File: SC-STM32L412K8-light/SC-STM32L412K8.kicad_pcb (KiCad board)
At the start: 2 copper layers, 31.6 x 15.1 mm, 62 parts, among them J1 usb, J11 Vibro, J12 +3v, J13 +vibro, J2 +29.6 SiPM, J3 TxD, J4 RxD, J5 SWDIO, J6 SWCLK, J7 +BAT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

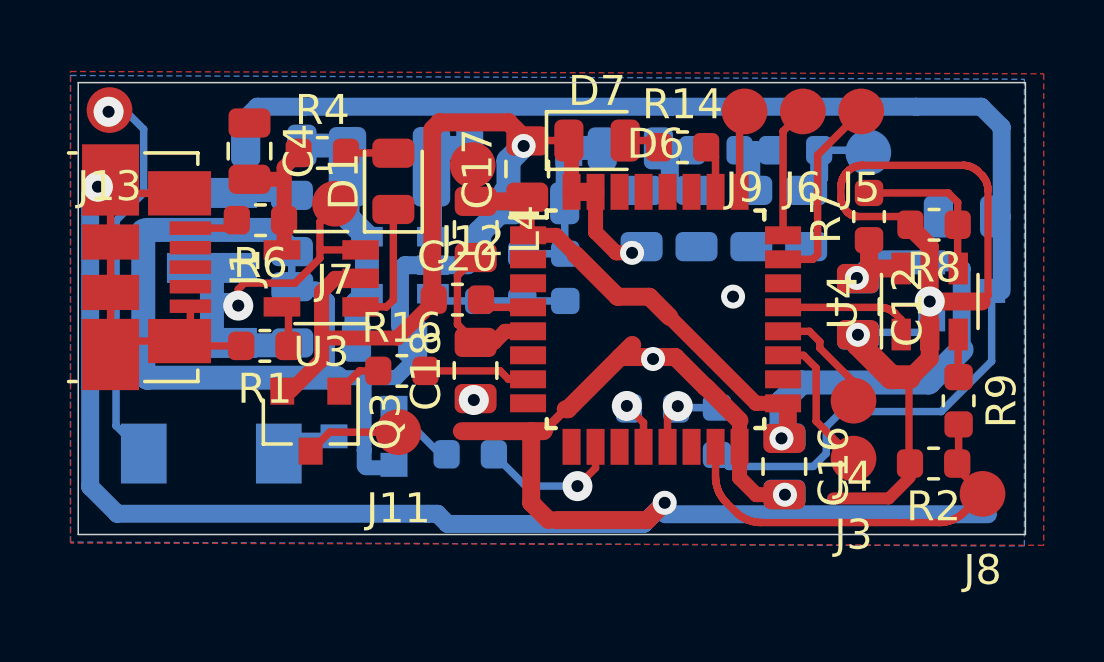
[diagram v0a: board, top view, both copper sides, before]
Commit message: изменено:      SC-STM32L412K8-light/SC-STM32L412K8.kicad_pcb 	изменено:      SC-STM32L412K8-light/SC-STM32L412K8.kicad_pcb-bak 	изменено:      SC-STM32L412K8-light/SC-STM32L412K8.net 	изменено:      SC-STM32L412K8-light/SC-STM32L412K8.sch 	изменено:      SC-STM32L412K8-light/SC-STM32L412K8.sch-bak 	изменено:      STM32L412K8code/Release/Core/Src/stm32l4xx_it.su
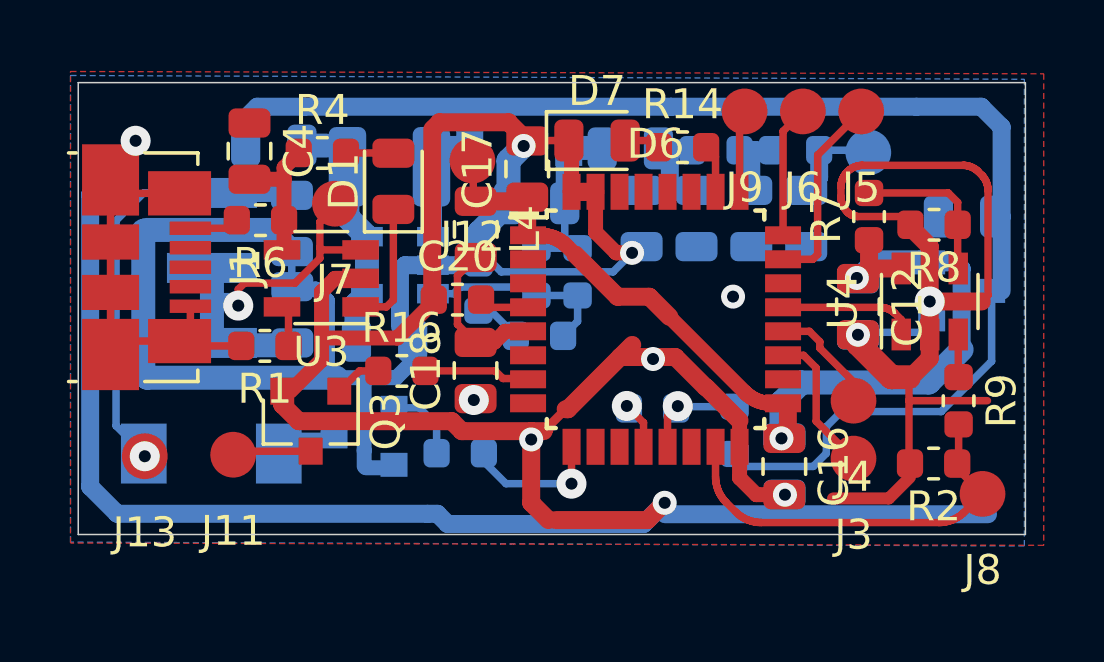
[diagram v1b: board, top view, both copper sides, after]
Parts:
- added R10: 1k*, Resistor_SMD:R_0603_1608Metric, B.Cu at (40.8, 59.7)
- moved J13 11.6 mm to (29.7, 65.3)
- moved J11 5.56 mm to (32.6, 65.3)
- moved R3 2.80 mm to (42.8, 61.3), turned to 180 degrees
- moved R19 0.58 mm to (49.3, 64.5)
- moved C5 0.51 mm to (42.7, 59.2)
- moved R5 0.45 mm to (44.1, 59.2)
- moved R15 0.33 mm to (40.2, 65.2)
- moved J12 0.15 mm to (40.6, 55.5)
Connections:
- D6 pad 10: Buzer -> (no net)
- D6 pad 9: (no net) -> Buzer
- R3 pad 2: GND -> Net-(R10-Pad1)
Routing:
- net GND: track 174.4 -> 189.3 mm, vias 10 -> 11
- net +BATT: track 65.6 -> 61.5 mm
- net Net-(C5-Pad2): track 4.51 -> 6.57 mm
- net Net-(R10-Pad1): track 0.00 -> 1.59 mm
- net bl: track 2.99 -> 3.56 mm
- net Net-(J11-Pad1): track 3.18 -> 2.63 mm

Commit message: изменено:      SC-STM32L412K8-light/SC-STM32L412K8-cache.lib 	изменено:      SC-STM32L412K8-light/SC-STM32L412K8.kicad_pcb 	изменено:      SC-STM32L412K8-light/SC-STM32L412K8.kicad_pcb-bak 	изменено:      SC-STM32L412K8-light/SC-STM32L412K8.net 	изменено:      SC-STM32L412K8-light/SC-STM32L412K8.sch 	изменено:      SC-STM32L412K8-light/SC-STM32L412K8.sch-bak
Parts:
- removed BZ1: Buzzer, My-library:BuzerSMD
- removed Q3: KT231Г9, Package_TO_SOT_SMD:SOT-23
- added J10: Buzzer, My-library:SMD-CONN, B.Cu at (36.6, 65.3)
- added Q1: 2N7002, Package_TO_SOT_SMD:SOT-23, F.Cu at (36.8, 64.2)
- added R12: 200, Resistor_SMD:R_0603_1608Metric, B.Cu at (38.1, 65.3)
- J11, J13: moved to B.Cu
- Q2: value KT231Г9 -> 2N7002
- R10: value 1k* -> 3k*
- R15, R16: value 4.7k -> 100k
- moved J13 11.0 mm to (31.4, 54.5)
- moved R15 4.63 mm to (44.7, 66.2), turned to 180 degrees
- moved Q2 3.59 mm to (40.3, 66.1)
- moved J11 2.03 mm to (34.6, 65.3)
- moved R10 1.64 mm to (40.6, 61.3), turned to 180 degrees
- moved R16 1.26 mm to (39.0, 63.5), turned to 90 degrees
- moved R19 1.07 mm to (49.2, 63.4), turned to 0 degrees
- moved R3 0.58 mm to (43.4, 61.3)
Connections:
- Q2 pad 1: Net-(Q2-Pad1) -> Buzer
- R15 pad 1: Net-(Q2-Pad1) -> GND
- R16 pad 1: Net-(Q3-Pad1) -> GND
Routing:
- net +BATT: track 61.5 -> 52.5 mm, vias 1 -> 0
- net GND: track 189.3 -> 193.2 mm, vias 11 -> 10
- net Net-(Q2-Pad1): track 2.60 -> 0.00 mm
- net Net-(J10-Pad1): track 0.00 -> 1.87 mm
- net Vibro: track 3.53 -> 5.14 mm
- net Net-(Q3-Pad1): track 1.58 -> 0.00 mm
- net Net-(Q2-Pad3): track 2.08 -> 1.13 mm
- net Net-(C12-Pad1): track 35.1 -> 34.4 mm
- net bl: track 3.56 -> 2.85 mm
- net Net-(J11-Pad1): track 2.63 -> 2.15 mm, vias 0 -> 1

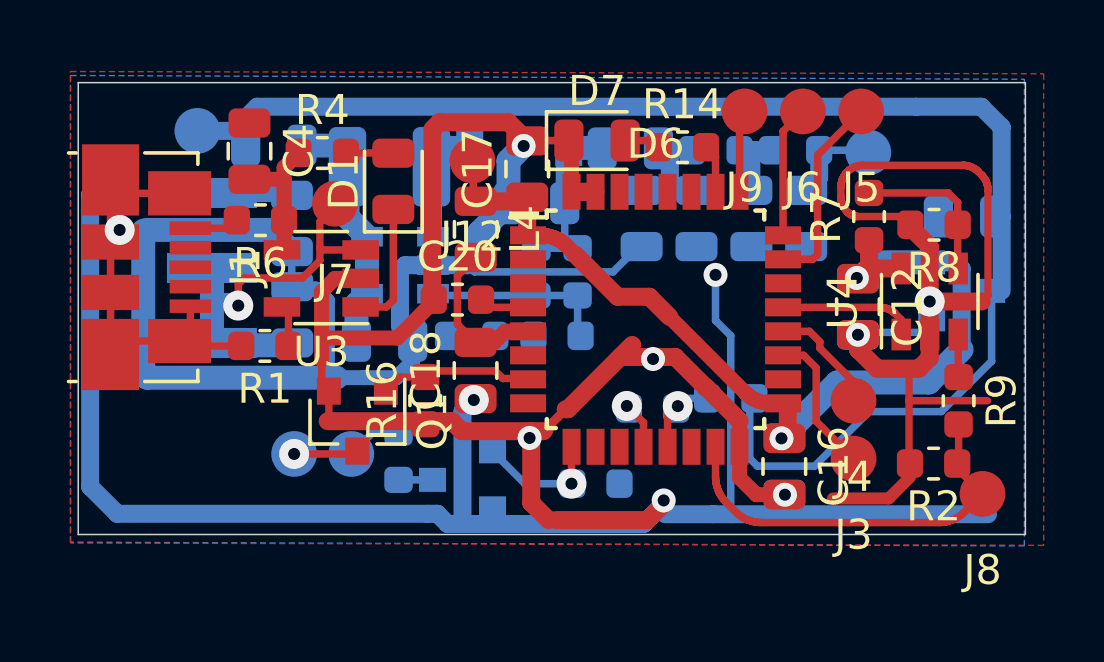
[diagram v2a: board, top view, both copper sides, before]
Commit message: modified:   FreeCAD/sc-box-7.FCStd 	modified:   FreeCAD/sc-box-7.stl 	modified:   FreeCAD/sc-cover-7.FCStd 	modified:   FreeCAD/sc-cover-7.FCStd1 	modified:   FreeCAD/sc-cover-7.stl 	modified:   SC-STM32L412K8-light/SC-STM32L412K8.kicad_pcb 	modified:   SC-STM32L412K8-light/SC-STM32L412K8.kicad_pcb-bak 	modified:   SC-STM32L412K8-light/SC-STM32L412K8.net 	modified:   SC-STM32L412K8-light/SC-STM32L412K8.sch 	modified:   SC-STM32L412K8-light/SC-STM32L412K8.sch-bak
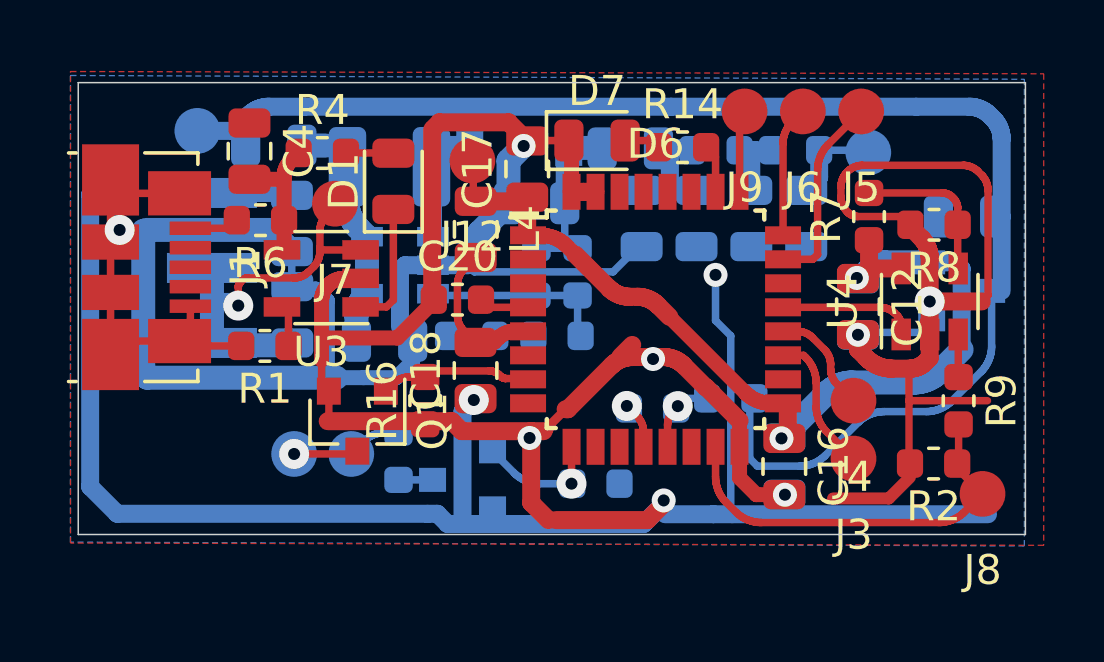
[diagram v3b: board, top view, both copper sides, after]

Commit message: изменено:      AndroidDoZer/app/src/main/java/ru/starline/dozer/FullscreenActivity2.java 	изменено:      AndroidDoZer/app/src/main/res/layout/activity_fullscreen2.xml 	изменено:      SC-STM32L412K8-light/SC-STM32L412K8-cache.lib 	изменено:      SC-STM32L412K8-light/SC-STM32L412K8.kicad_pcb 	изменено:      SC-STM32L412K8-light/SC-STM32L412K8.kicad_pcb-bak 	изменено:      SC-STM32L412K8-light/SC-STM32L412K8.net 	изменено:      SC-STM32L412K8-light/SC-STM32L412K8.sch 	изменено:      SC-STM32L412K8-light/SC-STM32L412K8.sch-bak 	изменено:      STM32L412K8code/.settings/language.settings.xml
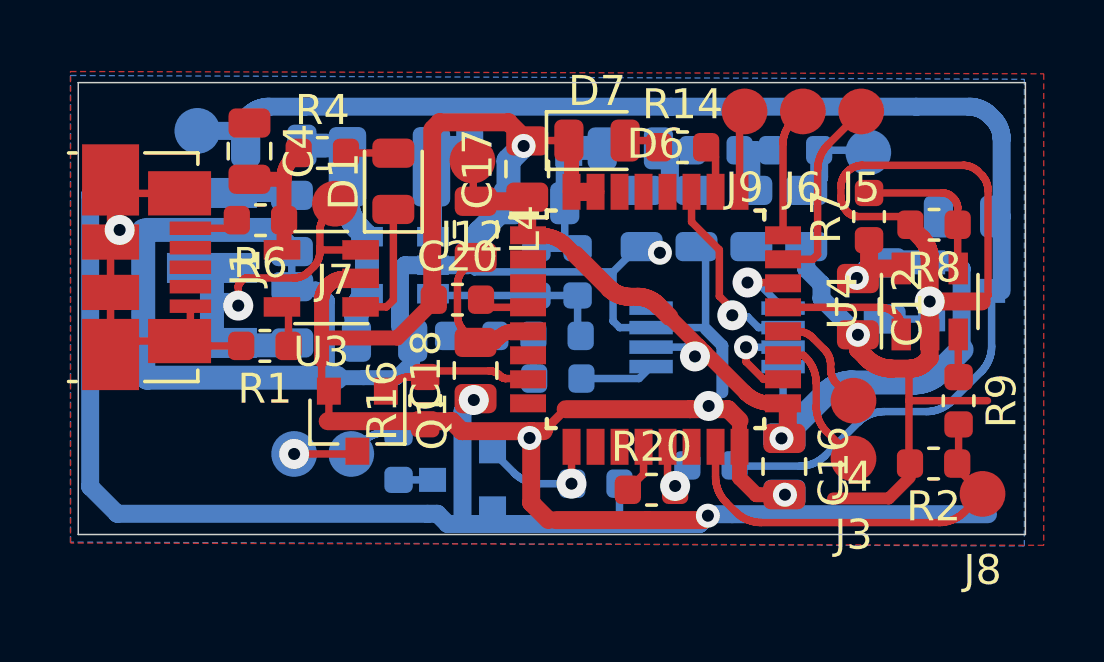
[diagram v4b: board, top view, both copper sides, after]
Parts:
- added D3: LTC1662CMS8, Package_SO:MSOP-8_3x3mm_P0.65mm, B.Cu at (48.7, 61.4)
- added R17: 100k, Resistor_SMD:R_0603_1608Metric, B.Cu at (43.4, 62.7)
- J3: value TxD -> TxD (20)
- J4: value RxD -> RxD (19)
- Q1, Q2: value 2N7002 -> IRLML6344
- R20: moved to F.Cu
- R8: value 4.7k -> 5.1k
- moved R20 2.71 mm to (46.6, 66.4)
- moved R19 2.33 mm to (48.5, 65.6)
- moved C2 1.04 mm to (54.3, 59.8)
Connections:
- net Net-(C12-Pad1) renamed +3V3
- net Net-(R10-Pad1) renamed Adjust
- D6 pad 18: (no net) -> DI
- D6 pad 22: (no net) -> CS
- D6 pad 27: (no net) -> SC
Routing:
- net SC: track 0.00 -> 6.46 mm, vias 0 -> 1
- net GND: track 193.0 -> 198.3 mm
- net +3V3: track 34.2 -> 38.4 mm, vias 2 -> 3
- net DI: track 0.00 -> 3.20 mm, vias 0 -> 1
- net CS: track 0.00 -> 2.58 mm, vias 0 -> 1
- net Net-(D3-Pad5): track 0.00 -> 2.49 mm
- net +BATT: track 52.2 -> 50.5 mm
- net Adjust: track 1.27 -> 2.70 mm
- net bl: track 2.82 -> 2.26 mm
- net com: track 1.56 -> 1.65 mm, vias 1 -> 0

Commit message: modified:   SC-STM32L412K8-light/SC-STM32L412K8.kicad_pcb 	modified:   SC-STM32L412K8-light/SC-STM32L412K8.kicad_pcb-bak
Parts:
- moved R20 0.24 mm to (46.3, 66.5)
